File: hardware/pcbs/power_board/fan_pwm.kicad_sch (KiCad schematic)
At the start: 5 parts

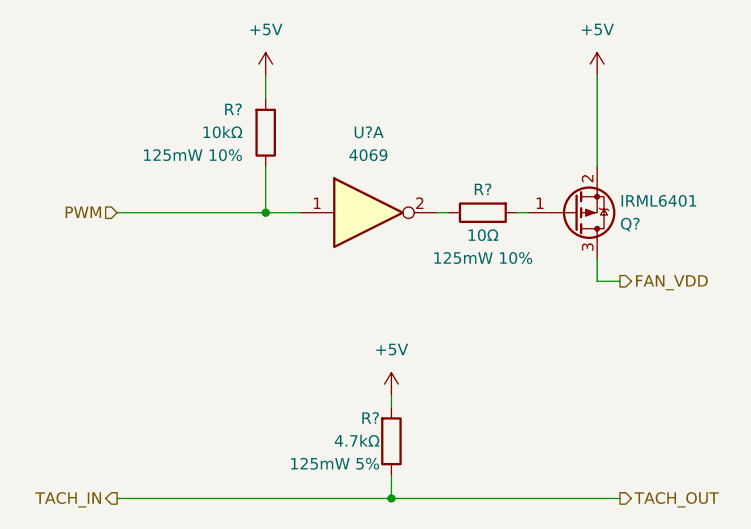
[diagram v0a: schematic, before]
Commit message: power_board: update components to new versions and annotate
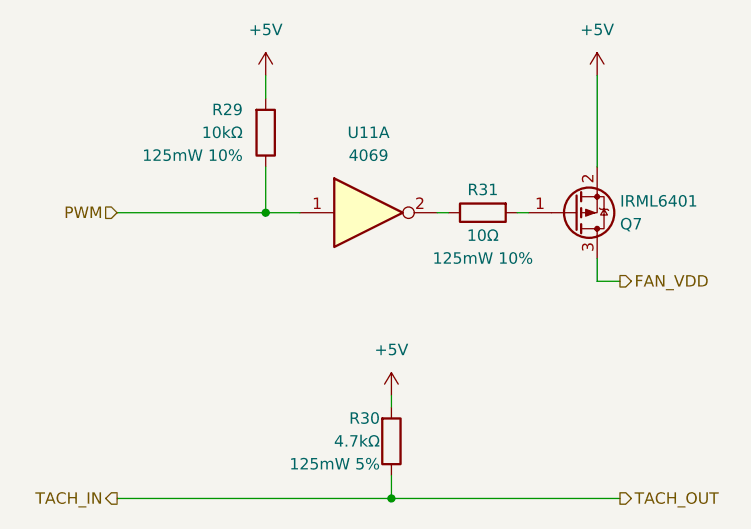
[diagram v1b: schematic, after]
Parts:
- U11: renamed from U?; footprint (none) -> Package_SO:SO-14_3.9x8.65mm_P1.27mm; Part (none) -> HEF4069UBT; Shop (none) -> https://store.comet.bg/Catalogue/Product/48094/
- gave numbers to parts that had none: 4
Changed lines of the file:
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@@
 		(on_board yes)
 		(dnp no)
-		(property "Reference" "R?"
+		(property "Reference" "R29"
 			(at 129.54 80.01 0)
 			(effects
@@
 			(project "power_board"
 				(path "/4b166175-80a4-48c6-994d-6e62a6160b87/f4395b92-97ec-456a-b4c2-238b75f494a2/1f2356c2-5114-44bd-9e00-8022e0f5b6a5"
-					(reference "R?")
+					(reference "R29")
 					(unit 1)
 				)
 				(path "/4b166175-80a4-48c6-994d-6e62a6160b87/f4395b92-97ec-456a-b4c2-238b75f494a2/ba1e0391-72e2-478c-ae36-437899b49871"
-					(reference "R?")
+					(reference "R32")
 					(unit 1)
 				)
 				(path "/4b166175-80a4-48c6-994d-6e62a6160b87/f4395b92-97ec-456a-b4c2-238b75f494a2/67d89172-f710-42f2-b66a-20a713f3ef78"
-					(reference "R?")
+					(reference "R47")
 					(unit 1)
 				)
 				(path "/4b166175-80a4-48c6-994d-6e62a6160b87/f4395b92-97ec-456a-b4c2-238b75f494a2/06607c2e-df57-4ef0-bf70-954d4a07371a"
-					(reference "R?")
+					(reference "R50")
 					(unit 1)
 				)
@@
 		(dnp no)
 		(fields_autoplaced yes)
-		(property "Reference" "U?"
+		(property "Reference" "U11"
 			(at 143.51 82.55 0)
 			(effects
@@
 			)
 		)
-		(property "Footprint" ""
+		(property "Footprint" "Package_SO:SO-14_3.9x8.65mm_P1.27mm"
 			(at 143.51 91.44 0)
 			(effects
@@
 		)
 		(property "Description" "Hex inverter"
+			(at 143.51 91.44 0)
+			(effects
+				(font
+					(size 1.27 1.27)
+				)
+				(hide yes)
+			)
+		)
+		(property "Part" "HEF4069UBT"
+			(at 143.51 91.44 0)
+			(effects
+				(font
+					(size 1.27 1.27)
+				)
+				(hide yes)
+			)
+		)
+		(property "Shop" "https://store.comet.bg/Catalogue/Product/48094/"
 			(at 143.51 91.44 0)
 			(effects
@@
 			(project "power_board"
 				(path "/4b166175-80a4-48c6-994d-6e62a6160b87/f4395b92-97ec-456a-b4c2-238b75f494a2/67d89172-f710-42f2-b66a-20a713f3ef78"
-					(reference "U?")
+					(reference "U11")
 					(unit 1)
 				)
 				(path "/4b166175-80a4-48c6-994d-6e62a6160b87/f4395b92-97ec-456a-b4c2-238b75f494a2/1f2356c2-5114-44bd-9e00-8022e0f5b6a5"
-					(reference "U?")
+					(reference "U11")
 					(unit 2)
 				)
 				(path "/4b166175-80a4-48c6-994d-6e62a6160b87/f4395b92-97ec-456a-b4c2-238b75f494a2/ba1e0391-72e2-478c-ae36-437899b49871"
-					(reference "U?")
+					(reference "U11")
 					(unit 3)
 				)
 				(path "/4b166175-80a4-48c6-994d-6e62a6160b87/f4395b92-97ec-456a-b4c2-238b75f494a2/06607c2e-df57-4ef0-bf70-954d4a07371a"
-					(reference "U?")
+					(reference "U11")
 					(unit 4)
 				)
@@
 		(on_board yes)
 		(dnp no)
-		(property "Reference" "R?"
+		(property "Reference" "R30"
 			(at 144.78 114.3 0)
 			(effects
@@
 			(project "power_board"
 				(path "/4b166175-80a4-48c6-994d-6e62a6160b87/f4395b92-97ec-456a-b4c2-238b75f494a2/1f2356c2-5114-44bd-9e00-8022e0f5b6a5"
-					(reference "R?")
+					(reference "R30")
 					(unit 1)
 				)
 				(path "/4b166175-80a4-48c6-994d-6e62a6160b87/f4395b92-97ec-456a-b4c2-238b75f494a2/ba1e0391-72e2-478c-ae36-437899b49871"
-					(reference "R?")
+					(reference "R33")
 					(unit 1)
 				)
 				(path "/4b166175-80a4-48c6-994d-6e62a6160b87/f4395b92-97ec-456a-b4c2-238b75f494a2/67d89172-f710-42f2-b66a-20a713f3ef78"
-					(reference "R?")
+					(reference "R48")
 					(unit 1)
 				)
 				(path "/4b166175-80a4-48c6-994d-6e62a6160b87/f4395b92-97ec-456a-b4c2-238b75f494a2/06607c2e-df57-4ef0-bf70-954d4a07371a"
-					(reference "R?")
+					(reference "R51")
 					(unit 1)
 				)
@@
 		(on_board yes)
 		(dnp no)
-		(property "Reference" "R?"
+		(property "Reference" "R31"
 			(at 156.21 88.9 90)
 			(effects
@@
 			(project "power_board"
 				(path "/4b166175-80a4-48c6-994d-6e62a6160b87/f4395b92-97ec-456a-b4c2-238b75f494a2/1f2356c2-5114-44bd-9e00-8022e0f5b6a5"
-					(reference "R?")
+					(reference "R31")
 					(unit 1)
 				)
 				(path "/4b166175-80a4-48c6-994d-6e62a6160b87/f4395b92-97ec-456a-b4c2-238b75f494a2/ba1e0391-72e2-478c-ae36-437899b49871"
-					(reference "R?")
+					(reference "R34")
 					(unit 1)
 				)
 				(path "/4b166175-80a4-48c6-994d-6e62a6160b87/f4395b92-97ec-456a-b4c2-238b75f494a2/67d89172-f710-42f2-b66a-20a713f3ef78"
-					(reference "R?")
+					(reference "R49")
 					(unit 1)
 				)
 				(path "/4b166175-80a4-48c6-994d-6e62a6160b87/f4395b92-97ec-456a-b4c2-238b75f494a2/06607c2e-df57-4ef0-bf70-954d4a07371a"
-					(reference "R?")
+					(reference "R52")
 					(unit 1)
 				)
@@
 		(dnp no)
 		(fields_autoplaced yes)
-		(property "Reference" "#PWR039"
+		(property "Reference" "#PWR054"
 			(at 146.05 115.57 0)
 			(effects
@@
 			(project "power_board"
 				(path "/4b166175-80a4-48c6-994d-6e62a6160b87/f4395b92-97ec-456a-b4c2-238b75f494a2/1f2356c2-5114-44bd-9e00-8022e0f5b6a5"
-					(reference "#PWR039")
+					(reference "#PWR054")
 					(unit 1)
 				)
 				(path "/4b166175-80a4-48c6-994d-6e62a6160b87/f4395b92-97ec-456a-b4c2-238b75f494a2/ba1e0391-72e2-478c-ae36-437899b49871"
-					(reference "#PWR040")
+					(reference "#PWR057")
 					(unit 1)
 				)
 				(path "/4b166175-80a4-48c6-994d-6e62a6160b87/f4395b92-97ec-456a-b4c2-238b75f494a2/67d89172-f710-42f2-b66a-20a713f3ef78"
-					(reference "#PWR041")
+					(reference "#PWR096")
 					(unit 1)
 				)
 				(path "/4b166175-80a4-48c6-994d-6e62a6160b87/f4395b92-97ec-456a-b4c2-238b75f494a2/06607c2e-df57-4ef0-bf70-954d4a07371a"
-					(reference "#PWR042")
+					(reference "#PWR099")
 					(unit 1)
 				)
@@
 		(on_board yes)
 		(dnp no)
-		(property "Reference" "Q?"
+		(property "Reference" "Q7"
 			(at 171.45 92.71 0)
 			(effects
@@
 			(project "power_board"
 				(path "/4b166175-80a4-48c6-994d-6e62a6160b87/f4395b92-97ec-456a-b4c2-238b75f494a2/67d89172-f710-42f2-b66a-20a713f3ef78"
-					(reference "Q?")
+					(reference "Q7")
+					(unit 1)
+				)
+				(path "/4b166175-80a4-48c6-994d-6e62a6160b87/f4395b92-97ec-456a-b4c2-238b75f494a2/1f2356c2-5114-44bd-9e00-8022e0f5b6a5"
+					(reference "Q2")
+					(unit 1)
+				)
+				(path "/4b166175-80a4-48c6-994d-6e62a6160b87/f4395b92-97ec-456a-b4c2-238b75f494a2/ba1e0391-72e2-478c-ae36-437899b49871"
+					(reference "Q3")
+					(unit 1)
+				)
+				(path "/4b166175-80a4-48c6-994d-6e62a6160b87/f4395b92-97ec-456a-b4c2-238b75f494a2/06607c2e-df57-4ef0-bf70-954d4a07371a"
+					(reference "Q8")
 					(unit 1)
 				)
@@
 		(dnp no)
 		(fields_autoplaced yes)
-		(property "Reference" "#PWR091"
+		(property "Reference" "#PWR055"
 			(at 168.91 80.01 0)
 			(effects
@@
 			(project "power_board"
 				(path "/4b166175-80a4-48c6-994d-6e62a6160b87/f4395b92-97ec-456a-b4c2-238b75f494a2/1f2356c2-5114-44bd-9e00-8022e0f5b6a5"
-					(reference "#PWR091")
+					(reference "#PWR055")
 					(unit 1)
 				)
 				(path "/4b166175-80a4-48c6-994d-6e62a6160b87/f4395b92-97ec-456a-b4c2-238b75f494a2/ba1e0391-72e2-478c-ae36-437899b49871"
-					(reference "#PWR092")
+					(reference "#PWR058")
 					(unit 1)
 				)
 				(path "/4b166175-80a4-48c6-994d-6e62a6160b87/f4395b92-97ec-456a-b4c2-238b75f494a2/67d89172-f710-42f2-b66a-20a713f3ef78"
-					(reference "#PWR093")
+					(reference "#PWR097")
 					(unit 1)
 				)
 				(path "/4b166175-80a4-48c6-994d-6e62a6160b87/f4395b92-97ec-456a-b4c2-238b75f494a2/06607c2e-df57-4ef0-bf70-954d4a07371a"
-					(reference "#PWR094")
+					(reference "#PWR0100")
 					(unit 1)
 				)
@@
 		(dnp no)
 		(fields_autoplaced yes)
-		(property "Reference" "#PWR044"
+		(property "Reference" "#PWR053"
 			(at 132.08 80.01 0)
 			(effects
@@
 			(project "power_board"
 				(path "/4b166175-80a4-48c6-994d-6e62a6160b87/f4395b92-97ec-456a-b4c2-238b75f494a2/1f2356c2-5114-44bd-9e00-8022e0f5b6a5"
-					(reference "#PWR044")
+					(reference "#PWR053")
 					(unit 1)
 				)
 				(path "/4b166175-80a4-48c6-994d-6e62a6160b87/f4395b92-97ec-456a-b4c2-238b75f494a2/ba1e0391-72e2-478c-ae36-437899b49871"
-					(reference "#PWR046")
+					(reference "#PWR056")
 					(unit 1)
 				)
 				(path "/4b166175-80a4-48c6-994d-6e62a6160b87/f4395b92-97ec-456a-b4c2-238b75f494a2/67d89172-f710-42f2-b66a-20a713f3ef78"
-					(reference "#PWR047")
+					(reference "#PWR095")
 					(unit 1)
 				)
 				(path "/4b166175-80a4-48c6-994d-6e62a6160b87/f4395b92-97ec-456a-b4c2-238b75f494a2/06607c2e-df57-4ef0-bf70-954d4a07371a"
-					(reference "#PWR090")
-					(unit 1)
-				)
+					(reference "#PWR098")
+					(unit 1)
+				)

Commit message: power_board: initial outline
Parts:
- Q7: LCSC (none) -> C20917
- R31: LCSC (none) -> C17415
- U11: LCSC (none) -> C551467
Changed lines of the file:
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@@
+			)
+		)
+		(property "LCSC" "C551467"
+			(at 143.51 91.44 0)
+			(effects
+				(font
+					(size 1.27 1.27)
+				)
+				(hide yes)
 			)
 		)
@@
 			)
 		)
-		(property "LCSC" ""
+		(property "LCSC" "C17415"
 			(at 156.21 91.44 0)
 			(effects
@@
 			(at 166.37 91.44 0)
 			(effects
+				(font
+					(size 1.27 1.27)
+				)
+				(hide yes)
+			)
+		)
+		(property "LCSC" "C20917"
+			(at 166.37 91.44 0)
+			(effects

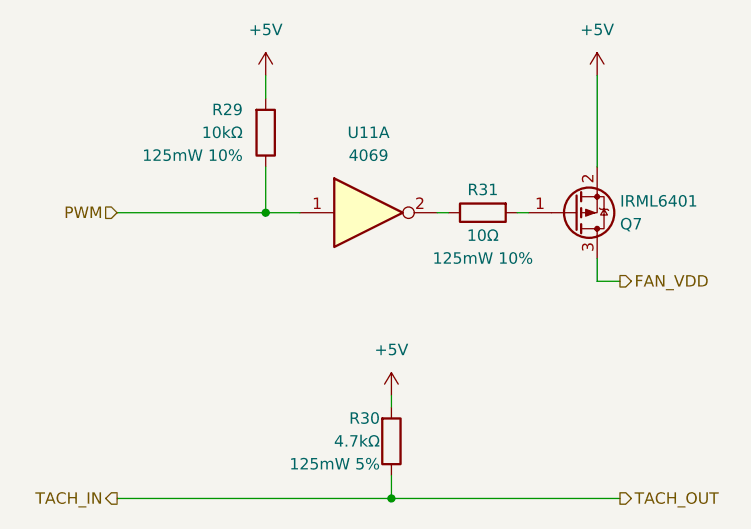
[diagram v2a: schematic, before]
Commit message: audio_board, power_board: update shop and part links
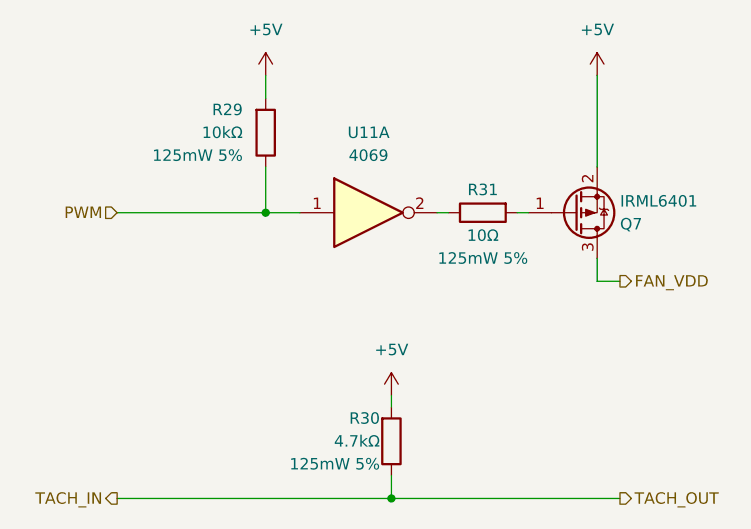
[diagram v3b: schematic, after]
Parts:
- R29: Info 125mW 10% -> 125mW 5%; Part (none) -> R 10kΩ 125mW 5% 0805
- R30: Part (none) -> R 4.7kΩ 125mW 5% 0805
- R31: Info 125mW 10% -> 125mW 5%; Part (none) -> R 10Ω 125mW 5% 0805
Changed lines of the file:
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@@
 			)
 		)
-		(property "Info" "125mW 10%"
+		(property "Info" "125mW 5%"
 			(at 129.54 85.09 0)
 			(effects
@@
 		)
 		(property "LCSC" "C17414"
+			(at 132.08 82.55 0)
+			(effects
+				(font
+					(size 1.27 1.27)
+				)
+				(hide yes)
+			)
+		)
+		(property "Part" "R 10kΩ 125mW 5% 0805"
 			(at 132.08 82.55 0)
 			(effects
@@
 			)
 		)
+		(property "Part" "R 4.7kΩ 125mW 5% 0805"
+			(at 146.05 116.84 0)
+			(effects
+				(font
+					(size 1.27 1.27)
+				)
+				(hide yes)
+			)
+		)
 		(pin "1"
 		)
@@
 			)
 		)
-		(property "Info" "125mW 10%"
+		(property "Info" "125mW 5%"
 			(at 156.21 96.52 90)
 			(effects
@@
 			(at 156.21 91.44 0)
 			(effects
+				(font
+					(size 1.27 1.27)
+				)
+				(hide yes)
+			)
+		)
+		(property "Part" "R 10Ω 125mW 5% 0805"
+			(at 156.21 91.44 0)
+			(effects

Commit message: power_board: holes with larger keepouts
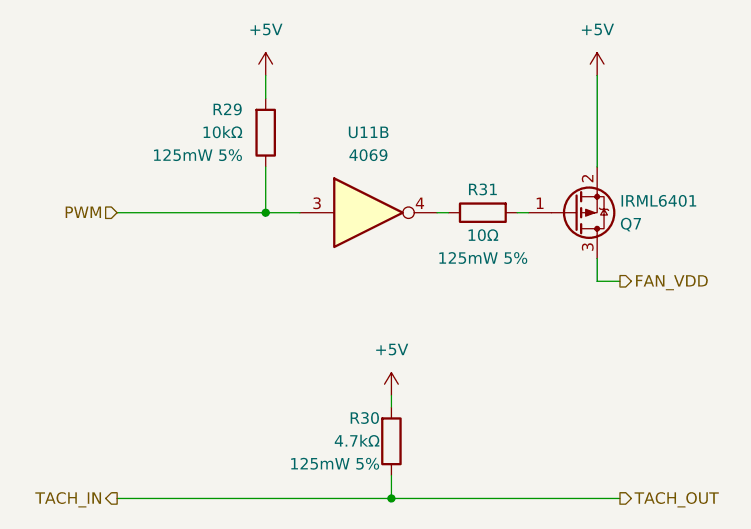
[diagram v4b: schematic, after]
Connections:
- net PWM: now also U11.3; no longer U11.1
- net at R31.1: now also U11.4; no longer U11.2
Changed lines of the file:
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@@
 		(lib_id "4xxx:4069")
 		(at 143.51 91.44 0)
-		(unit 1)
+		(unit 2)
 		(exclude_from_sim no)
 		(in_bom yes)
@@
 				(path "/4b166175-80a4-48c6-994d-6e62a6160b87/f4395b92-97ec-456a-b4c2-238b75f494a2/67d89172-f710-42f2-b66a-20a713f3ef78"
 					(reference "U11")
-					(unit 1)
+					(unit 2)
 				)
 				(path "/4b166175-80a4-48c6-994d-6e62a6160b87/f4395b92-97ec-456a-b4c2-238b75f494a2/1f2356c2-5114-44bd-9e00-8022e0f5b6a5"
 					(reference "U11")
-					(unit 2)
+					(unit 4)
 				)
 				(path "/4b166175-80a4-48c6-994d-6e62a6160b87/f4395b92-97ec-456a-b4c2-238b75f494a2/ba1e0391-72e2-478c-ae36-437899b49871"
 					(reference "U11")
-					(unit 3)
+					(unit 1)
 				)
 				(path "/4b166175-80a4-48c6-994d-6e62a6160b87/f4395b92-97ec-456a-b4c2-238b75f494a2/06607c2e-df57-4ef0-bf70-954d4a07371a"
 					(reference "U11")
-					(unit 4)
+					(unit 3)
 				)
 			)

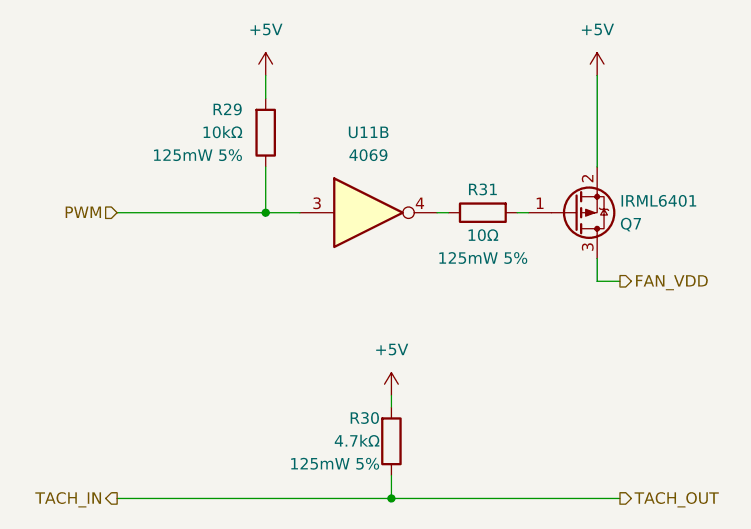
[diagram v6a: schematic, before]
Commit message: power_board: final-ish shape
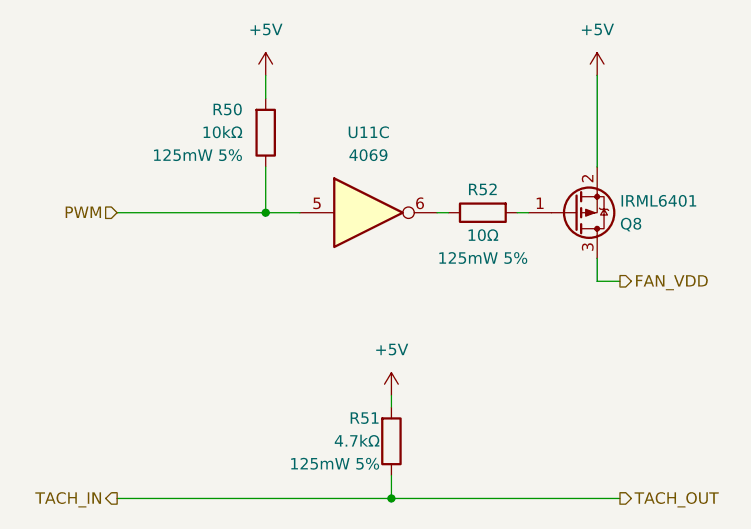
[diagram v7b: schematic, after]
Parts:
- renumbered Q7 to Q8, R29 to R50, R30 to R51, R31 to R52
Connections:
- net PWM: now also U11.5; no longer U11.3
- net at R52.1: now also U11.6; no longer U11.4
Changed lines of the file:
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@@
 		(on_board yes)
 		(dnp no)
-		(property "Reference" "R29"
+		(property "Reference" "R50"
 			(at 129.54 80.01 0)
 			(effects
@@
 		(lib_id "4xxx:4069")
 		(at 143.51 91.44 0)
-		(unit 2)
+		(unit 3)
 		(exclude_from_sim no)
 		(in_bom yes)
@@
 				(path "/4b166175-80a4-48c6-994d-6e62a6160b87/f4395b92-97ec-456a-b4c2-238b75f494a2/1f2356c2-5114-44bd-9e00-8022e0f5b6a5"
 					(reference "U11")
-					(unit 4)
+					(unit 2)
 				)
 				(path "/4b166175-80a4-48c6-994d-6e62a6160b87/f4395b92-97ec-456a-b4c2-238b75f494a2/67d89172-f710-42f2-b66a-20a713f3ef78"
 					(reference "U11")
-					(unit 2)
+					(unit 4)
 				)
 				(path "/4b166175-80a4-48c6-994d-6e62a6160b87/f4395b92-97ec-456a-b4c2-238b75f494a2/ba1e0391-72e2-478c-ae36-437899b49871"
@@
 		(on_board yes)
 		(dnp no)
-		(property "Reference" "R30"
+		(property "Reference" "R51"
 			(at 144.78 114.3 0)
 			(effects
@@
 		(on_board yes)
 		(dnp no)
-		(property "Reference" "R31"
+		(property "Reference" "R52"
 			(at 156.21 88.9 90)
 			(effects
@@
 		(dnp no)
 		(fields_autoplaced yes)
-		(property "Reference" "#PWR055"
+		(property "Reference" "#PWR098"
 			(at 146.05 115.57 0)
 			(effects
@@
 			(project "power_board"
 				(path "/4b166175-80a4-48c6-994d-6e62a6160b87/f4395b92-97ec-456a-b4c2-238b75f494a2/06607c2e-df57-4ef0-bf70-954d4a07371a"
-					(reference "#PWR099")
+					(reference "#PWR098")
 					(unit 1)
 				)
 				(path "/4b166175-80a4-48c6-994d-6e62a6160b87/f4395b92-97ec-456a-b4c2-238b75f494a2/1f2356c2-5114-44bd-9e00-8022e0f5b6a5"
-					(reference "#PWR055")
+					(reference "#PWR054")
 					(unit 1)
 				)
 				(path "/4b166175-80a4-48c6-994d-6e62a6160b87/f4395b92-97ec-456a-b4c2-238b75f494a2/67d89172-f710-42f2-b66a-20a713f3ef78"
-					(reference "#PWR096")
+					(reference "#PWR095")
 					(unit 1)
 				)
 				(path "/4b166175-80a4-48c6-994d-6e62a6160b87/f4395b92-97ec-456a-b4c2-238b75f494a2/ba1e0391-72e2-478c-ae36-437899b49871"
-					(reference "#PWR058")
+					(reference "#PWR057")
 					(unit 1)
 				)
@@
 		(on_board yes)
 		(dnp no)
-		(property "Reference" "Q7"
+		(property "Reference" "Q8"
 			(at 171.45 92.71 0)
 			(effects
@@
 		(dnp no)
 		(fields_autoplaced yes)
-		(property "Reference" "#PWR056"
+		(property "Reference" "#PWR099"
 			(at 168.91 80.01 0)
 			(effects
@@
 			(project "power_board"
 				(path "/4b166175-80a4-48c6-994d-6e62a6160b87/f4395b92-97ec-456a-b4c2-238b75f494a2/06607c2e-df57-4ef0-bf70-954d4a07371a"
-					(reference "#PWR0100")
+					(reference "#PWR099")
 					(unit 1)
 				)
 				(path "/4b166175-80a4-48c6-994d-6e62a6160b87/f4395b92-97ec-456a-b4c2-238b75f494a2/1f2356c2-5114-44bd-9e00-8022e0f5b6a5"
-					(reference "#PWR056")
+					(reference "#PWR055")
 					(unit 1)
 				)
 				(path "/4b166175-80a4-48c6-994d-6e62a6160b87/f4395b92-97ec-456a-b4c2-238b75f494a2/67d89172-f710-42f2-b66a-20a713f3ef78"
-					(reference "#PWR097")
+					(reference "#PWR096")
 					(unit 1)
 				)
 				(path "/4b166175-80a4-48c6-994d-6e62a6160b87/f4395b92-97ec-456a-b4c2-238b75f494a2/ba1e0391-72e2-478c-ae36-437899b49871"
-					(reference "#PWR059")
+					(reference "#PWR058")
 					(unit 1)
 				)
@@
 		(dnp no)
 		(fields_autoplaced yes)
-		(property "Reference" "#PWR054"
+		(property "Reference" "#PWR097"
 			(at 132.08 80.01 0)
 			(effects
@@
 			(project "power_board"
 				(path "/4b166175-80a4-48c6-994d-6e62a6160b87/f4395b92-97ec-456a-b4c2-238b75f494a2/06607c2e-df57-4ef0-bf70-954d4a07371a"
-					(reference "#PWR098")
+					(reference "#PWR097")
 					(unit 1)
 				)
 				(path "/4b166175-80a4-48c6-994d-6e62a6160b87/f4395b92-97ec-456a-b4c2-238b75f494a2/1f2356c2-5114-44bd-9e00-8022e0f5b6a5"
-					(reference "#PWR054")
+					(reference "#PWR053")
 					(unit 1)
 				)
 				(path "/4b166175-80a4-48c6-994d-6e62a6160b87/f4395b92-97ec-456a-b4c2-238b75f494a2/67d89172-f710-42f2-b66a-20a713f3ef78"
-					(reference "#PWR095")
+					(reference "#PWR094")
 					(unit 1)
 				)
 				(path "/4b166175-80a4-48c6-994d-6e62a6160b87/f4395b92-97ec-456a-b4c2-238b75f494a2/ba1e0391-72e2-478c-ae36-437899b49871"
-					(reference "#PWR057")
-					(unit 1)
-				)
+					(reference "#PWR056")
+					(unit 1)
+				)
